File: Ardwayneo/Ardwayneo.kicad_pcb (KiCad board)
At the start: 2 copper layers, 40.9 x 25.7 mm, 17 parts, among them J1 Digital Pins, J2 ICSP, J3 Serial, J4 I2C, U1 24LC1025, U2 24LC1025, U3 ATMEGA328P-AU, U4 DS1337S+, Y1 Crystal 32MHz, Y2 Crystal 16MHz

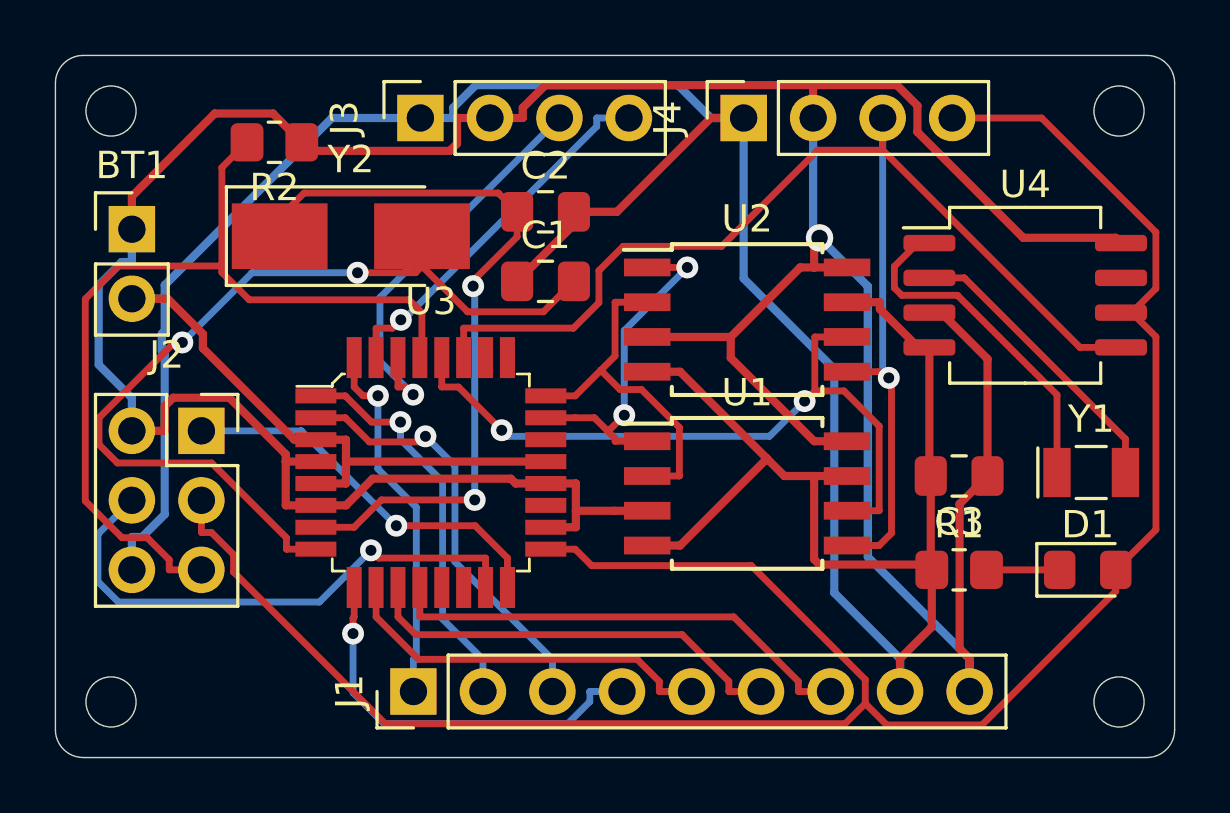
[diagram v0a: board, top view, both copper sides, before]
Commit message: Used autorouter to create 4 layer board
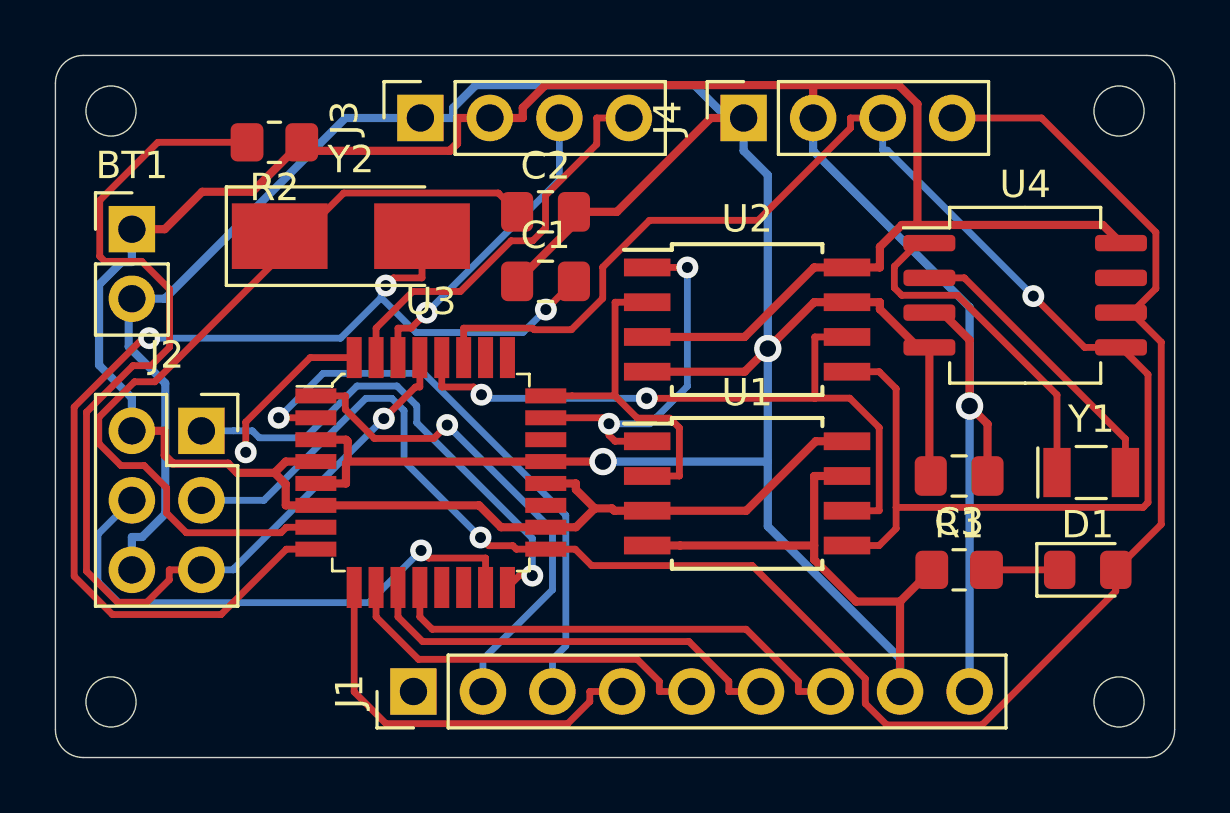
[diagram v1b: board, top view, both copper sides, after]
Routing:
- net /SCK: track 79.0 -> 67.7 mm, vias 0 -> 1
- net Net-(C1-Pad2): track 32.6 -> 41.3 mm, vias 2 -> 3
- net /RESET: track 33.1 -> 40.5 mm, vias 0 -> 1
- net /SDA: track 51.4 -> 57.9 mm
- net /D4: track 15.7 -> 21.3 mm
- net /Vcc: track 135.2 -> 130.5 mm
- net /MISO: track 14.2 -> 18.1 mm
- net /D2: track 13.5 -> 17.3 mm
- net /D3: track 14.6 -> 18.3 mm
- net /RX: track 15.1 -> 11.5 mm
- net GNDPWR: track 130.8 -> 127.3 mm, vias 0 -> 2
- net Net-(C2-Pad1): track 27.4 -> 30.6 mm, vias 2 -> 0
- net /SCL: track 26.4 -> 25.3 mm
- net /TX: track 13.7 -> 14.8 mm, vias 1 -> 0
- net /ADDS1: track 12.8 -> 13.5 mm
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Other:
- copper layers 2 -> 4
